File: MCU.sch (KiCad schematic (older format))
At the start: 38 parts, among them J5 ARM_JTAG_SWD_10, U5 STM32F769IITx

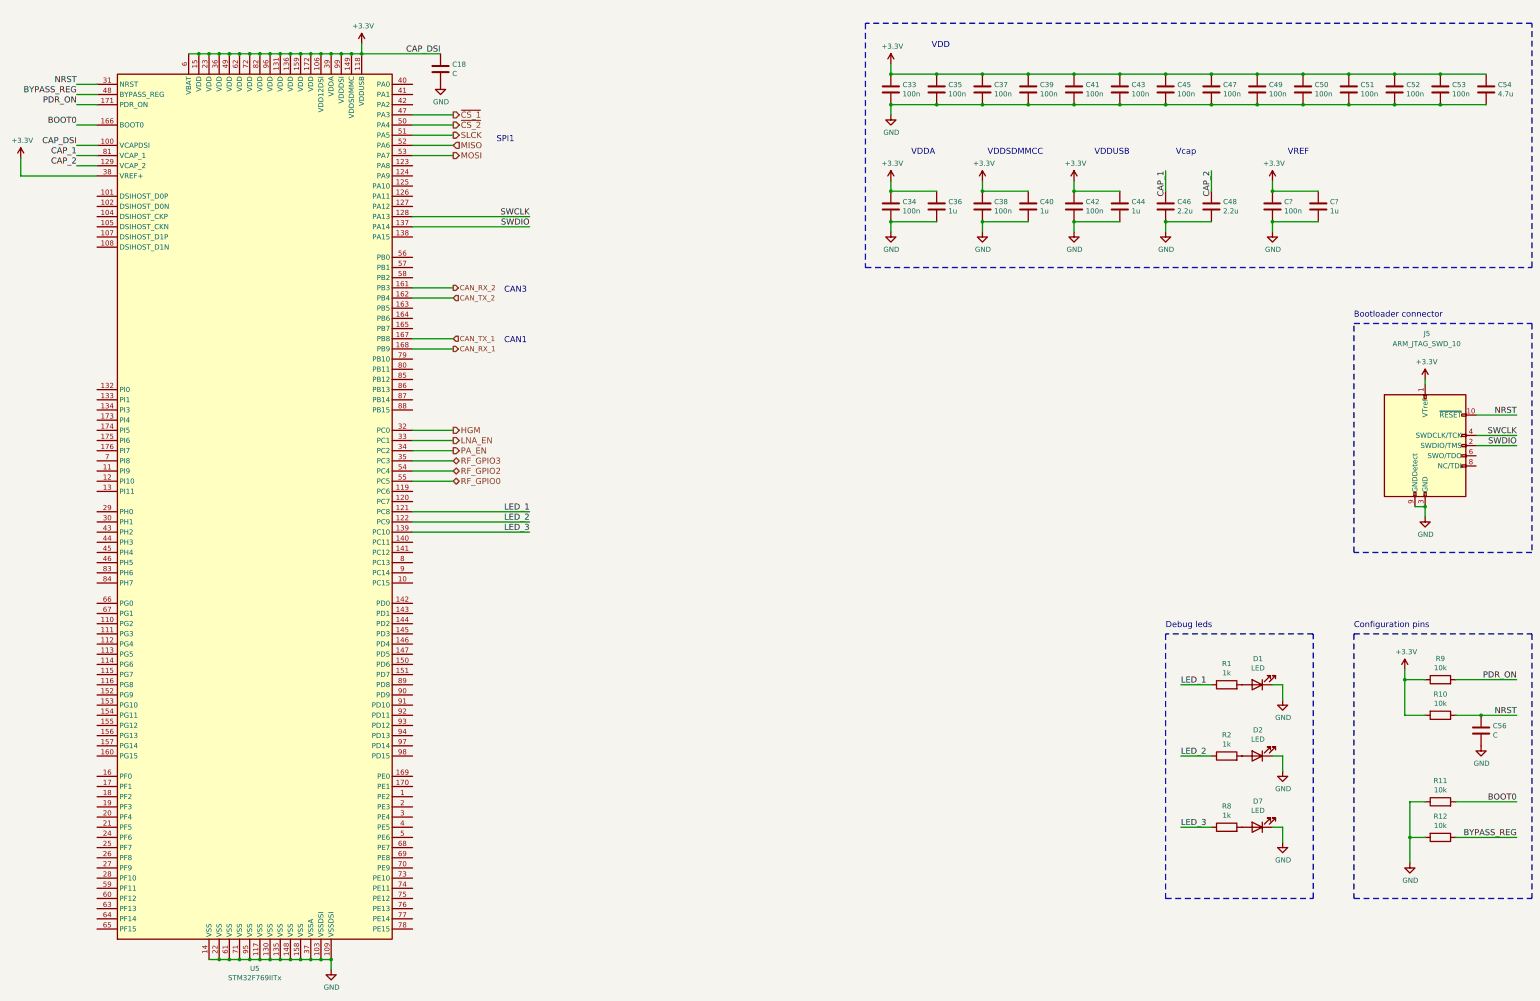
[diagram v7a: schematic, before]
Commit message: Changed to F4 MCU
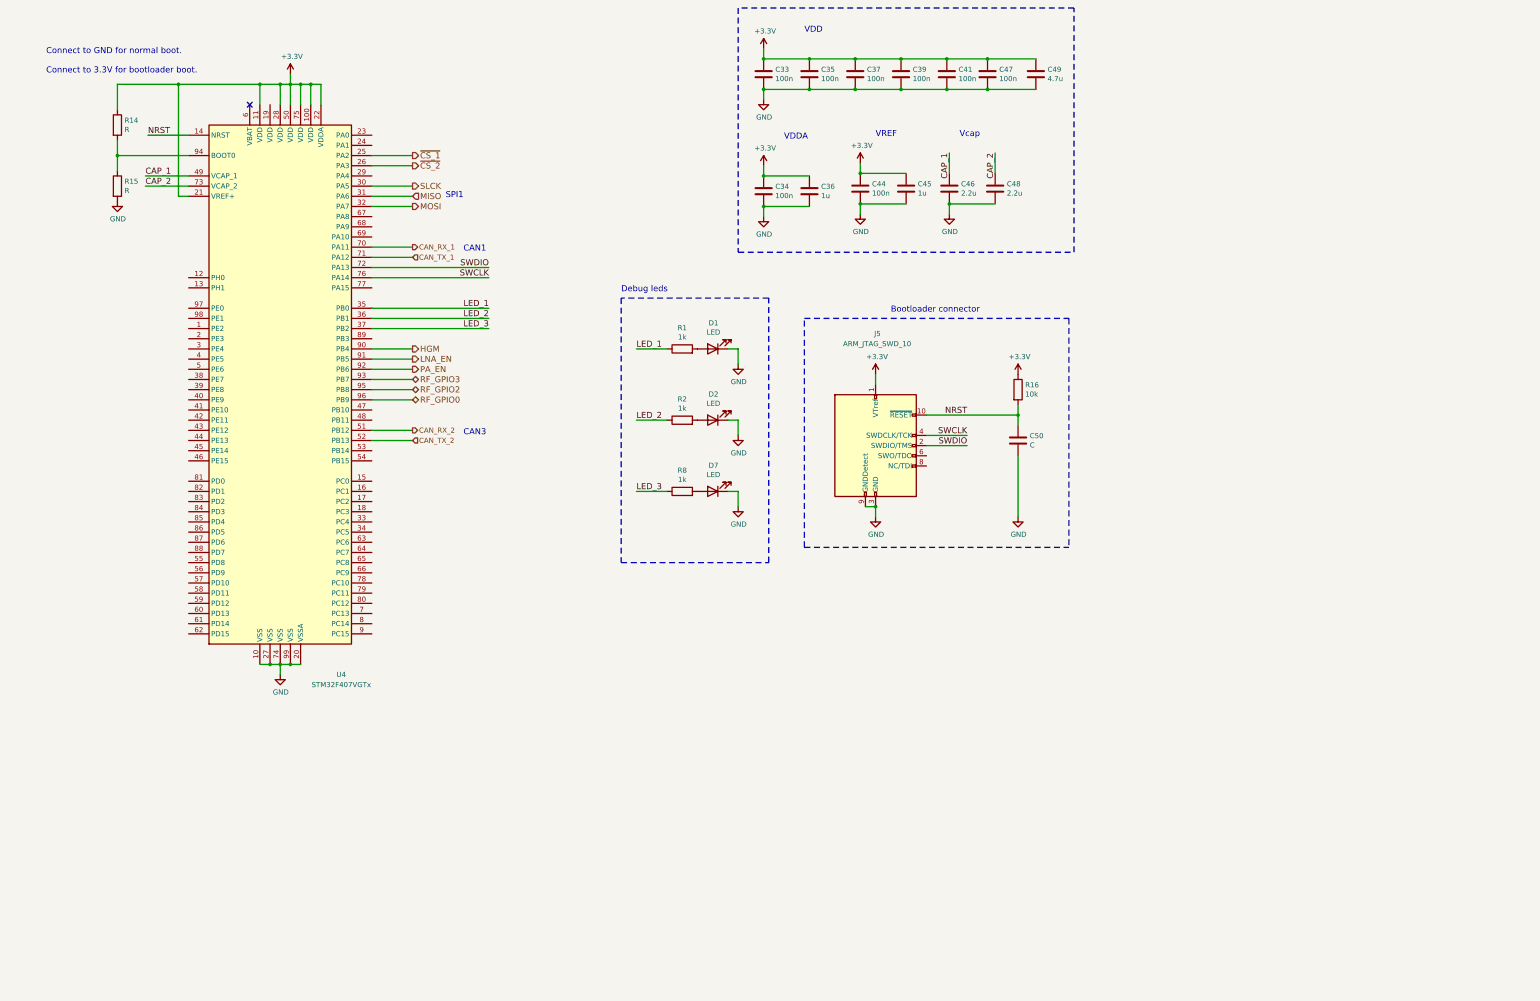
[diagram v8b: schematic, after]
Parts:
- removed C18, C56: C, Capacitor_SMD:C_0603_1608Metric, symbol Device:C
- removed C38, C42, C43, C45, C51, C52, C53: 100n, Capacitor_SMD:C_0603_1608Metric, symbol Device:C
- removed C40, C44: 1u, Capacitor_SMD:C_0603_1608Metric, symbol Device:C
- removed C54: 4.7u, Capacitor_SMD:C_0603_1608Metric, symbol Device:C
- removed R10, R11, R12, R9: 10k, Resistor_SMD:R_0603_1608Metric, symbol Device:R
- removed U5: STM32F769IITx, Package_QFP:LQFP-176_24x24mm_P0.5mm, symbol MCU_ST_STM32F7:STM32F769IITx
- added R14, R15: R, symbol Device:R
- added R16: 10k, symbol Device:R
- added U4: STM32F407VGTx, Package_QFP:LQFP-100_14x14mm_P0.5mm, symbol MCU_ST_STM32F4:STM32F407VGTx
- C49: value 100n -> 4.7u
- C50: value 100n -> C; footprint Capacitor_SMD:C_0603_1608Metric -> (none)
- gave numbers to parts that had none: 2
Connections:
- net +3V3: now also R14.1, R16.1, U4.100 (VDD), U4.11 (VDD), U4.21 (VREF+), U4.22 (VDDA), U4.28 (VDD), U4.50 (VDD), U4.75 (VDD); no longer C50.1
- net CAN_RX_1: now also U4.70 (PA11)
- net CAN_RX_2: now also U4.51 (PB12)
- net CAN_TX_1: now also U4.71 (PA12)
- net CAN_TX_2: now also U4.52 (PB13)
- net CAP_1: now also U4.49 (VCAP_1)
- net CAP_2: now also U4.73 (VCAP_2)
- net GND: now also R15.2, U4.10 (VSS), U4.20 (VSSA), U4.27 (VSS), U4.74 (VSS), U4.99 (VSS)
- net HGM: now also U4.90 (PB4)
- net LED_1: now also U4.35 (PB0)
- net LED_2: now also U4.36 (PB1)
- net LED_3: now also U4.37 (PB2)
- net LNA_EN: now also U4.91 (PB5)
- net MISO: now also U4.31 (PA6)
- net MOSI: now also U4.32 (PA7)
- net NRST: now also C50.1, R16.2, U4.14 (NRST)
- net PA_EN: now also U4.92 (PB6)
- net RF_GPIO0: now also U4.96 (PB9)
- net RF_GPIO2: now also U4.95 (PB8)
- net RF_GPIO3: now also U4.93 (PB7)
- net SLCK: now also U4.30 (PA5)
- net SWCLK: now also U4.76 (PA14)
- net SWDIO: now also U4.72 (PA13)
- net ~CS_1: now also U4.25 (PA2)
- net ~CS_2: now also U4.26 (PA3)
- new net: R14.2, R15.1, U4.94 (BOOT0)
- no-connect marks 0 -> 1
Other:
- note added: "Connect to GND for normal boot.\n\nConnect to 3.3V for bootloader boot."
- note removed: "Configuration pins\n"
- note removed: "VDDSDMMCC"
- note removed: "VDDUSB"
- moved on the sheet: C33, C34, C35, C36, C37, C39, C41, C44, C45, C46, C48, D1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
